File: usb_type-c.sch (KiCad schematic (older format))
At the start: 1 part, among them P1 12401548E4#2A

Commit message: Changed USB connector to SMD version
There's now quite a bit of stuff located under the USB connector.  A lot
of manufacturers mark that area as a keep-out zone, but luckily,
Amphenol is not one of them.
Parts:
- removed P1: 12401548E4#2A, pd-buddy:Amphenol-12401548E4#2A, symbol 12401548E4#2A
- added P1: 12401610E4#2A, pd-buddy:Amphenol-12401610E4#2A, symbol 12401610E4#2A
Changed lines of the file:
@@
 Comment4 ""
 $EndDescr
-$Comp
-L 12401548E4#2A P1
-U 1 1 588FA6A2
-P 4100 2350
-AR Path="/588FA6A2" Ref="P1"  Part="1"
-AR Path="/588FA5F7/588FA6A2" Ref="P1"  Part="1"
-F 0 "P1" H 4400 1600 60  0000 C CNN
-F 1 "12401548E4#2A" H 4100 3000 60  0000 C CNN
-F 2 "pd-buddy:Amphenol-12401548E4#2A" H 4100 2350 60  0001 C CNN
-F 3 "https://www.amphenolcanada.com/StockAvailabilityPrice.aspx?From=&PartNum=12401548E4%7e2A" H 4400 1600 60  0001 C CNN
-	1    4100 2350
-	1    0    0    -1
-$EndComp
 NoConn ~ 4700 1950
 NoConn ~ 4700 2050
@@
 	1    0    0    -1
 $EndComp
+$Comp
+L 12401610E4#2A P1
+U 1 1 58F76BCA
+P 4100 2350
+F 0 "P1" H 4400 1600 60  0000 C CNN
+F 1 "12401610E4#2A" H 4100 3000 60  0000 C CNN
+F 2 "pd-buddy:Amphenol-12401610E4#2A" H 4100 2350 60  0001 C CNN
+F 3 "https://www.amphenolcanada.com/StockAvailabilityPrice.aspx?From=&PartNum=12401610E4%7e2A" H 4400 1600 60  0001 C CNN
+	1    4100 2350
+	1    0    0    -1
+$EndComp

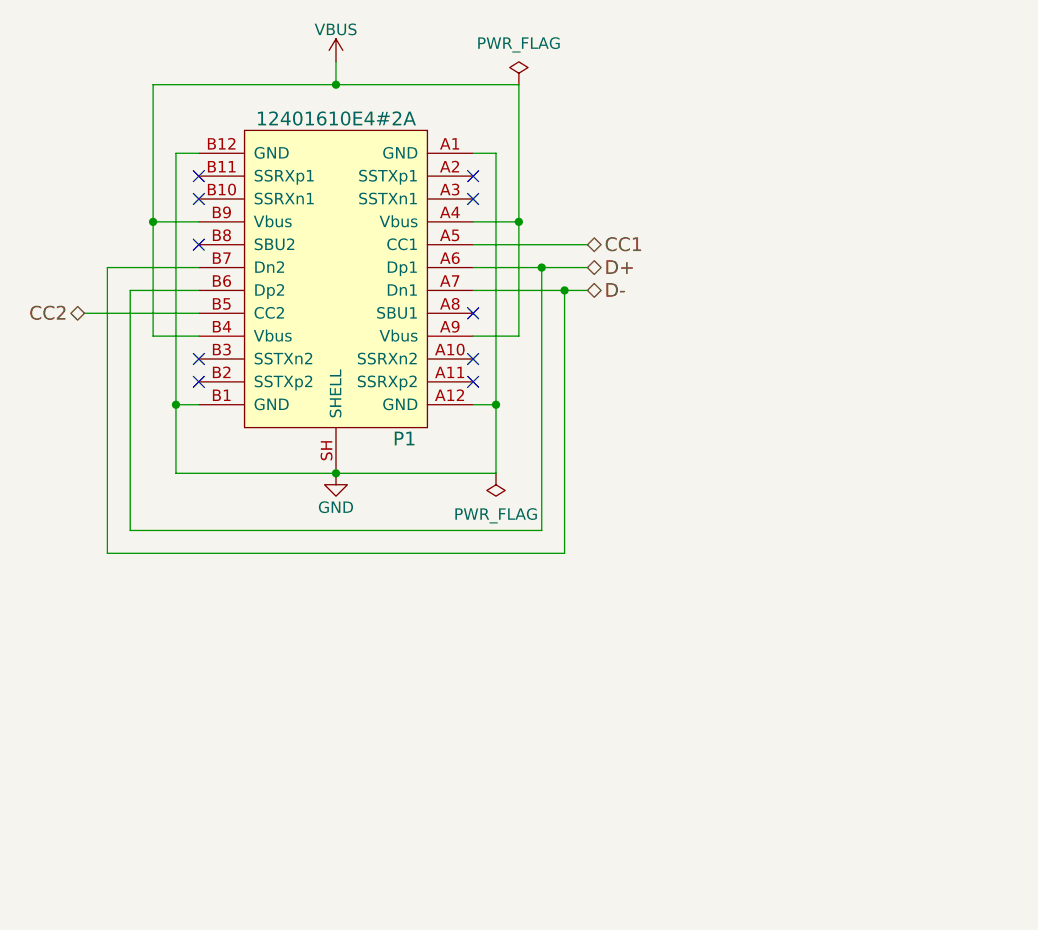
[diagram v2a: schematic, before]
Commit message: Use new USB Type-C schematic symbol
The footprints haven't been merged yet, but the symbol has.  Therefore,
I updated the footprint in the pd-buddy library to match the new symbol
(changed shield pin number to S1) and changed the schematic to have the
new connector symbol.  The board looks the same except that a couple
references changed.
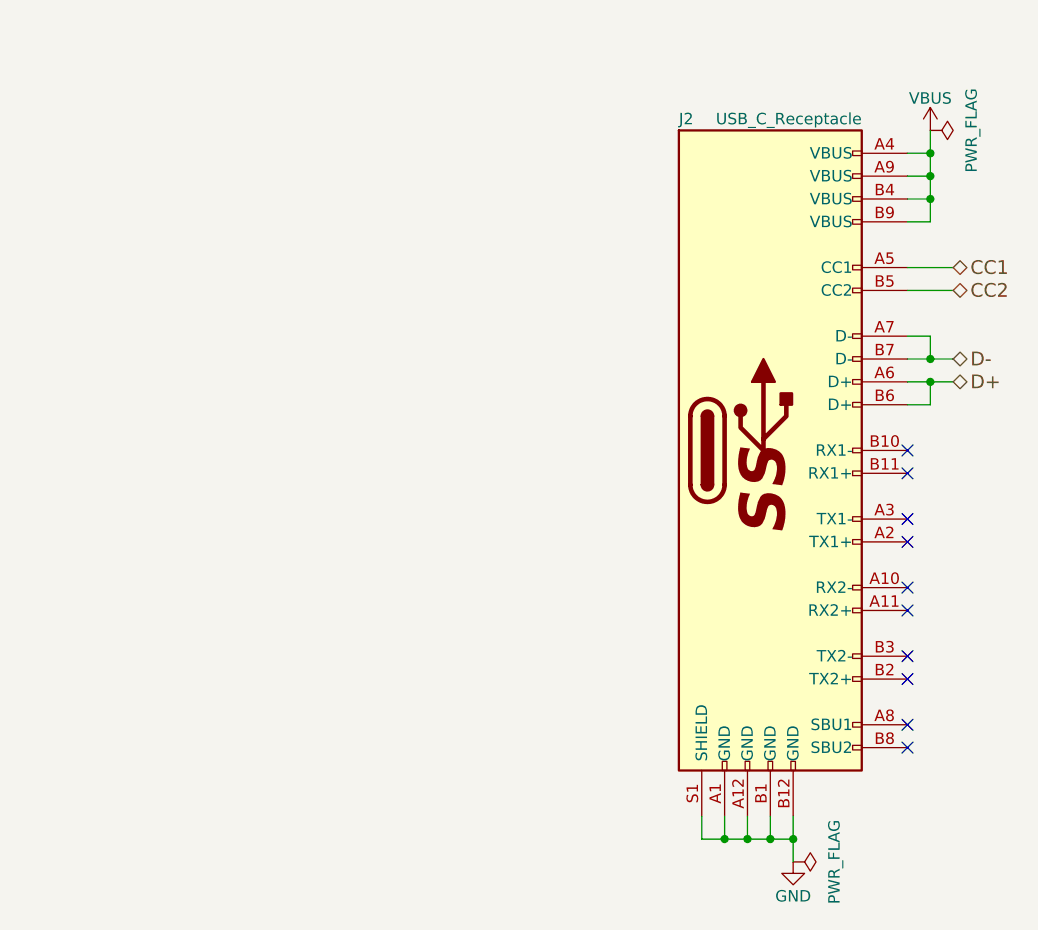
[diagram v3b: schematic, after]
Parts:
- removed P1: 12401610E4#2A, pd-buddy:Amphenol-12401610E4#2A, symbol 12401610E4#2A
- added J2: USB_C_Receptacle, pd-buddy:Amphenol-12401610E4#2A, symbol USB_C_Receptacle
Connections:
- net CC1: now also J2.A5 (CC1)
- net CC2: now also J2.B5 (CC2)
- net D+: now also J2.A6 (D+), J2.B6 (D+)
- net D-: now also J2.A7 (D-), J2.B7 (D-)
- net GND: now also J2.A1 (GND), J2.A12 (GND), J2.B1 (GND), J2.B12 (GND), J2.S1 (SHIELD)
- net VBUS: now also J2.A4 (VBUS), J2.A9 (VBUS), J2.B4 (VBUS), J2.B9 (VBUS)
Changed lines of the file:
@@
 Comment4 ""
 $EndDescr
-NoConn ~ 4700 1950
-NoConn ~ 4700 2050
-NoConn ~ 3500 1950
-NoConn ~ 3500 2050
-NoConn ~ 3500 2250
-NoConn ~ 4700 2550
-NoConn ~ 4700 2750
-NoConn ~ 4700 2850
-NoConn ~ 3500 2850
-NoConn ~ 3500 2750
-Wire Wire Line
-	4700 1850 4800 1850
-Wire Wire Line
-	4800 1850 4800 3250
-Wire Wire Line
-	4800 3250 3400 3250
-Wire Wire Line
-	4700 2950 4800 2950
-Connection ~ 4800 2950
-Wire Wire Line
-	3400 3250 3400 1850
-Wire Wire Line
-	3400 2950 3500 2950
-Connection ~ 4100 3250
-Wire Wire Line
-	3400 1850 3500 1850
-Connection ~ 3400 2950
+Text HLabel 6800 2350 2    60   BiDi ~ 0
+CC1
+Text HLabel 6800 2450 2    60   BiDi ~ 0
+CC2
+Text HLabel 6800 2850 2    60   BiDi ~ 0
+D+
+Text HLabel 6800 2750 2    60   BiDi ~ 0
+D-
 $Comp
-L GND #PWR035
-U 1 1 588FA6DC
-P 4100 3250
-F 0 "#PWR035" H 4100 3000 50  0001 C CNN
-F 1 "GND" H 4100 3100 50  0000 C CNN
-F 2 "" H 4100 3250 50  0000 C CNN
-F 3 "" H 4100 3250 50  0000 C CNN
-	1    4100 3250
+L USB_C_Receptacle J2
+U 1 1 59147856
+P 6000 3150
+F 0 "J2" H 5600 4600 50  0000 L CNN
+F 1 "USB_C_Receptacle" H 6400 4600 50  0000 R CNN
+F 2 "pd-buddy:Amphenol-12401610E4#2A" H 6150 3150 50  0001 C CNN
+F 3 "" H 6150 3150 50  0001 C CNN
+	1    6000 3150
+	1    0    0    -1
+$EndComp
+$Comp
+L VBUS #PWR035
+U 1 1 591478E7
+P 6700 1750
+F 0 "#PWR035" H 6700 1600 50  0001 C CNN
+F 1 "VBUS" H 6700 1890 50  0000 C CNN
+F 2 "" H 6700 1750 50  0000 C CNN
+F 3 "" H 6700 1750 50  0000 C CNN
+	1    6700 1750
 	1    0    0    -1
 $EndComp
 Wire Wire Line
-	4700 2150 4900 2150
+	6700 2150 6600 2150
 Wire Wire Line
-	4900 1550 4900 2650
+	6700 1750 6700 2150
 Wire Wire Line
-	4900 2650 4700 2650
+	6600 2050 6700 2050
+Connection ~ 6700 2050
 Wire Wire Line
-	3300 2650 3500 2650
+	6600 1950 6700 1950
+Connection ~ 6700 1950
 Wire Wire Line
-	3300 1550 3300 2650
-Wire Wire Line
-	3300 2150 3500 2150
-Wire Wire Line
-	3300 1550 4900 1550
-Connection ~ 3300 2150
-Connection ~ 4900 2150
+	6600 1850 6700 1850
+Connection ~ 6700 1850
 $Comp
-L VBUS #PWR036
-U 1 1 588FA72C
-P 4100 1450
-F 0 "#PWR036" H 4100 1300 50  0001 C CNN
-F 1 "VBUS" H 4100 1590 50  0000 C CNN
-F 2 "" H 4100 1450 50  0000 C CNN
-F 3 "" H 4100 1450 50  0000 C CNN
-	1    4100 1450
-	1    0    0    -1
+L PWR_FLAG #FLG036
+U 1 1 591479A3
+P 6700 1750
+F 0 "#FLG036" H 6700 1845 50  0001 C CNN
+F 1 "PWR_FLAG" H 6700 1930 50  0000 C CNN
+F 2 "" H 6700 1750 50  0000 C CNN
+F 3 "" H 6700 1750 50  0000 C CNN
+	1    6700 1750
+	0    1    1    0
 $EndComp
 Wire Wire Line
-	4100 1450 4100 1550
-Connection ~ 4100 1550
+	6600 2350 6800 2350
 Wire Wire Line
-	4700 2250 5200 2250
-Text HLabel 5200 2250 2    60   BiDi ~ 0
-CC1
-Text HLabel 3000 2550 0    60   BiDi ~ 0
-CC2
+	6800 2450 6600 2450
 Wire Wire Line
-	3000 2550 3500 2550
+	6600 2750 6800 2750
 Wire Wire Line
-	3500 2450 3200 2450
+	6600 2850 6800 2850
 Wire Wire Line
-	3200 2450 3200 3500
+	6600 2950 6700 2950
 Wire Wire Line
-	3200 3500 5000 3500
+	6700 2950 6700 2850
+Connection ~ 6700 2850
 Wire Wire Line
-	5000 3500 5000 2350
+	6600 2650 6700 2650
 Wire Wire Line
-	4700 2350 5200 2350
-Connection ~ 5000 2350
+	6700 2650 6700 2750
+Connection ~ 6700 2750
+NoConn ~ 6600 3150
+NoConn ~ 6600 3250
+NoConn ~ 6600 3450
+NoConn ~ 6600 3550
+NoConn ~ 6600 3750
+NoConn ~ 6600 3850
+NoConn ~ 6600 4050
+NoConn ~ 6600 4150
+NoConn ~ 6600 4350
+NoConn ~ 6600 4450
 Wire Wire Line
-	3500 2350 3100 2350
+	5700 4750 5700 4850
 Wire Wire Line
-	3100 2350 3100 3600
+	5700 4850 6100 4850
 Wire Wire Line
-	3100 3600 5100 3600
-Wire Wire Line
-	5100 3600 5100 2450
-Wire Wire Line
-	4700 2450 5200 2450
-Connection ~ 5100 2450
-Text HLabel 5200 2350 2    60   BiDi ~ 0
-D+
-Text HLabel 5200 2450 2    60   BiDi ~ 0
-D-
+	6100 4750 6100 4950
 $Comp
-L PWR_FLAG #FLG037
-U 1 1 588FBE9F
-P 4800 3250
-F 0 "#FLG037" H 4800 3345 50  0001 C CNN
-F 1 "PWR_FLAG" H 4800 3430 50  0000 C CNN
-F 2 "" H 4800 3250 50  0000 C CNN
-F 3 "" H 4800 3250 50  0000 C CNN
-	1    4800 3250
-	-1   0    0    1
+L GND #PWR037
+U 1 1 59147BA2
+P 6100 4950
+F 0 "#PWR037" H 6100 4700 50  0001 C CNN
+F 1 "GND" H 6100 4800 50  0000 C CNN
+F 2 "" H 6100 4950 50  0000 C CNN
+F 3 "" H 6100 4950 50  0000 C CNN
+	1    6100 4950
+	1    0    0    -1
 $EndComp
 $Comp
 L PWR_FLAG #FLG038
-U 1 1 588FBEB8
-P 4900 1550
-F 0 "#FLG038" H 4900 1645 50  0001 C CNN
-F 1 "PWR_FLAG" H 4900 1730 50  0000 C CNN
-F 2 "" H 4900 1550 50  0000 C CNN
-F 3 "" H 4900 1550 50  0000 C CNN
-	1    4900 1550
-	1    0    0    -1
+U 1 1 59147BB3
+P 6100 4950
+F 0 "#FLG038" H 6100 5045 50  0001 C CNN
+F 1 "PWR_FLAG" H 6100 5130 50  0000 C CNN
+F 2 "" H 6100 4950 50  0000 C CNN
+F 3 "" H 6100 4950 50  0000 C CNN
+	1    6100 4950
+	0    1    1    0
 $EndComp
-$Comp
-L 12401610E4#2A P1
-U 1 1 58F76BCA
-P 4100 2350
-F 0 "P1" H 4400 1600 60  0000 C CNN
-F 1 "12401610E4#2A" H 4100 3000 60  0000 C CNN
-F 2 "pd-buddy:Amphenol-12401610E4#2A" H 4100 2350 60  0001 C CNN
-F 3 "https://www.amphenolcanada.com/StockAvailabilityPrice.aspx?From=&PartNum=12401610E4%7e2A" H 4400 1600 60  0001 C CNN
-	1    4100 2350
-	1    0    0    -1
-$EndComp
+Connection ~ 6100 4850
+Wire Wire Line
+	6000 4850 6000 4750
+Connection ~ 6000 4850
+Wire Wire Line
+	5900 4750 5900 4850
+Connection ~ 5900 4850
+Wire Wire Line
+	5800 4750 5800 4850
+Connection ~ 5800 4850
 $EndSCHEMATC
